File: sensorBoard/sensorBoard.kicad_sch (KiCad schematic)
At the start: 10 parts, among them J1 Conn_01x08, J3 Conn_01x07, J4 Conn_01x04, J5 Conn_01x05, J6 Conn_01x02, J7 Conn_01x04, J8 Conn_01x03, U2 LD1117S33TR_SOT223

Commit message: added the footprints, connectors left
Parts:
- C1, C2: footprint (none) -> Capacitor_SMD:C_0805_2012Metric
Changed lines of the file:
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@@
 			)
 		)
-		(property "Footprint" ""
+		(property "Footprint" "Capacitor_SMD:C_0805_2012Metric"
 			(at 27.94 170.18 0)
 			(effects
@@
 			)
 		)
-		(property "Footprint" ""
+		(property "Footprint" "Capacitor_SMD:C_0805_2012Metric"
 			(at 60.96 168.91 0)
 			(effects

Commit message: started the layout
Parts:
- removed J1: Conn_01x08, symbol Connector_Generic:Conn_01x08
- removed J7: Conn_01x04, symbol Connector_Generic:Conn_01x04
- added H1, H2, H3, H4: MountingHole_Pad, MountingHole:MountingHole_4.3mm_M4_Pad_Via, symbol Mechanical:MountingHole_Pad
- added J1: Conn_01x04, Connector_Phoenix_MC_HighVoltage:PhoenixContact_MCV_1,5_4-G-5.08_1x04_P5.08mm_Vertical, symbol Connector_Generic:Conn_01x04
- added J7: Conn_01x02, Connector_Phoenix_MC_HighVoltage:PhoenixContact_MCV_1,5_2-G-5.08_1x02_P5.08mm_Vertical, symbol Connector_Generic:Conn_01x02
- J3: footprint (none) -> Connector_PinHeader_2.54mm:PinHeader_1x07_P2.54mm_Vertical
- J4: footprint (none) -> Connector_Phoenix_MC_HighVoltage:PhoenixContact_MCV_1,5_4-G-5.08_1x04_P5.08mm_Vertical
- J5: footprint (none) -> heder box:662105145021
- J6: footprint (none) -> heder box:662102145021
- J8: footprint (none) -> heder box:662103145021
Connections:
- net GND: now also H1.1, H2.1, H3.1, H4.1, J1.2 (Pin_2), J1.3 (Pin_3)
- net Protection/12V_IN: now also J1.4 (Pin_4)
- net Protection/5V_IN: now also J1.1 (Pin_1)
- new net Commutation/POLE+: J7.1 (Pin_1)
- new net Commutation/POLE-: J7.2 (Pin_2)
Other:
- sheet Commutation ports: added POLE+, POLE-; removed POLE_1, POLE_1_EN, POLE_2, POLE_2_EN
- sheet microcontroller ports: added none; removed POLE_1_EN, POLE_2_EN

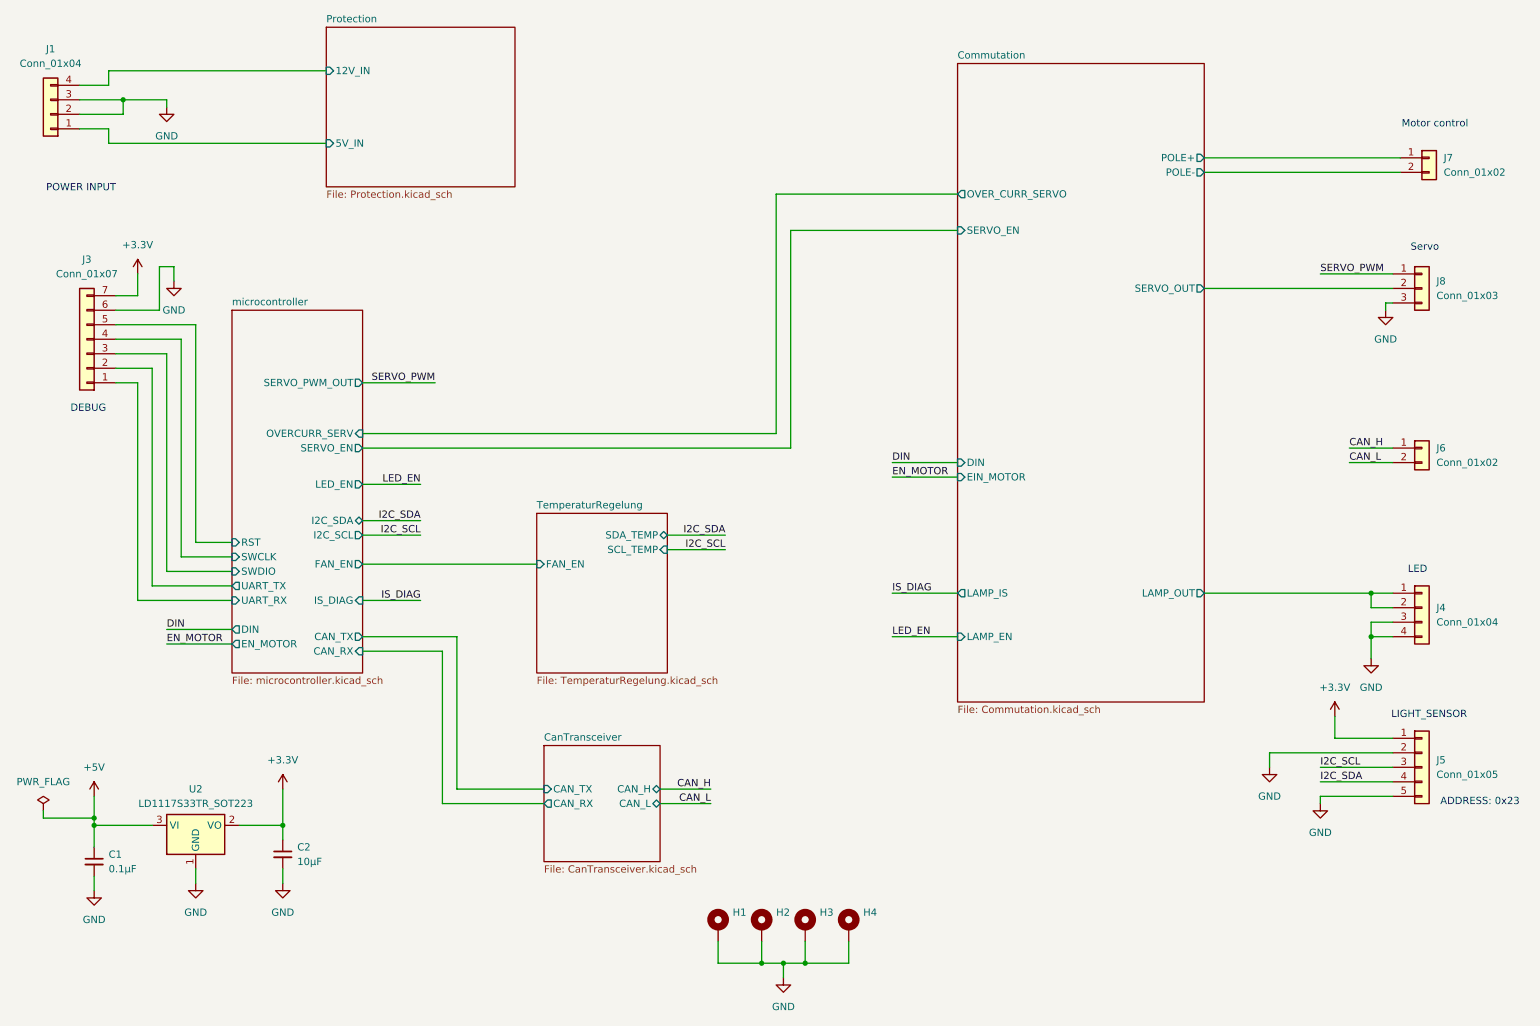
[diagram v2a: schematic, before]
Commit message: new two separate pcbs
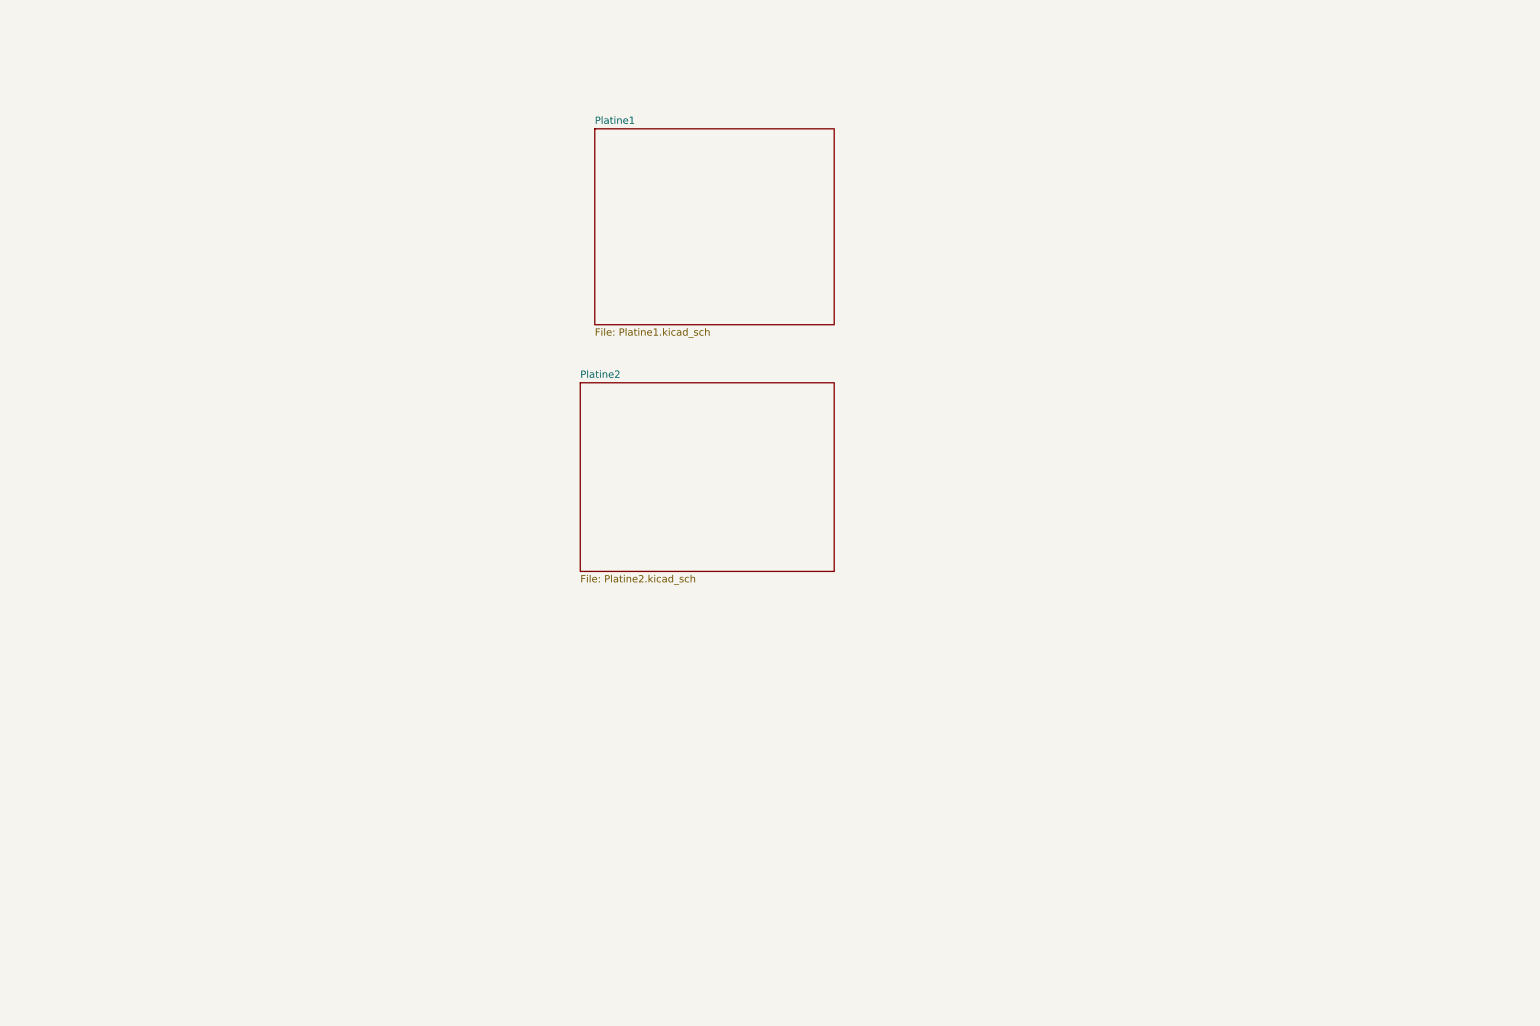
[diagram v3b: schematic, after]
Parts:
- removed C1: 0.1µF, Capacitor_SMD:C_0805_2012Metric, symbol Device:C_Small
- removed C2: 10µF, Capacitor_SMD:C_0805_2012Metric, symbol Device:C_Small
- removed H1, H2, H3, H4: MountingHole_Pad, MountingHole:MountingHole_4.3mm_M4_Pad_Via, symbol Mechanical:MountingHole_Pad
- removed J1, J4: Conn_01x04, Connector_Phoenix_MC_HighVoltage:PhoenixContact_MCV_1,5_4-G-5.08_1x04_P5.08mm_Vertical, symbol Connector_Generic:Conn_01x04
- removed J3: Conn_01x07, Connector_PinHeader_2.54mm:PinHeader_1x07_P2.54mm_Vertical, symbol Connector_Generic:Conn_01x07
- removed J5: Conn_01x05, heder box:662105145021, symbol Connector_Generic:Conn_01x05
- removed J6: Conn_01x02, heder box:662102145021, symbol Connector_Generic:Conn_01x02
- removed J7: Conn_01x02, Connector_Phoenix_MC_HighVoltage:PhoenixContact_MCV_1,5_2-G-5.08_1x02_P5.08mm_Vertical, symbol Connector_Generic:Conn_01x02
- removed J8: Conn_01x03, heder box:662103145021, symbol Connector_Generic:Conn_01x03
- removed U2: LD1117S33TR_SOT223, Package_TO_SOT_SMD:SOT-223-3_TabPin2, symbol Regulator_Linear:LD1117S33TR_SOT223
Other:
- removed sheet CanTransceiver
- removed sheet Commutation
- removed sheet Protection
- removed sheet TemperaturRegelung
- removed sheet microcontroller
- added sheet Platine1 (Platine1.kicad_sch)
- added sheet Platine2 (Platine2.kicad_sch)
- note removed: "ADDRESS: 0x23"
- note removed: "DEBUG"
- note removed: "LED"
- note removed: "LIGHT_SENSOR"
- note removed: "Motor control"
- note removed: "POWER INPUT"
- note removed: "Servo"

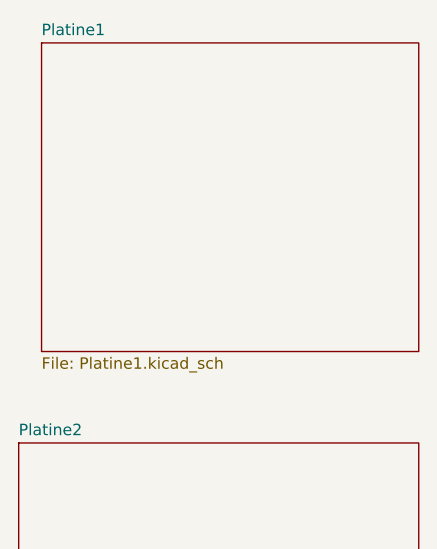
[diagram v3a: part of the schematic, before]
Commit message: Das erstes PCB ist fast fertig. Die Vias waren auf die Platine platziert und Poligon war gefüllt.
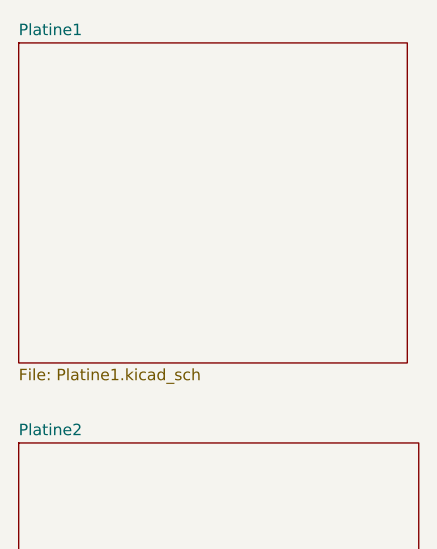
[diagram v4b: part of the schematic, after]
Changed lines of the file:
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@@
 	)
 	(sheet
-		(at 115.57 41.91)
-		(size 41.91 34.29)
+		(at 113.03 41.91)
+		(size 43.18 35.56)
 		(fields_autoplaced yes)
 		(stroke
@@
 		)
 		(property "Sheetname" "Platine1"
-			(at 115.57 41.1984 0)
+			(at 113.03 41.1984 0)
 			(effects
 				(font
@@
 		)
 		(property "Sheetfile" "Platine1.kicad_sch"
-			(at 115.57 76.7846 0)
+			(at 113.03 78.0546 0)
 			(effects
 				(font

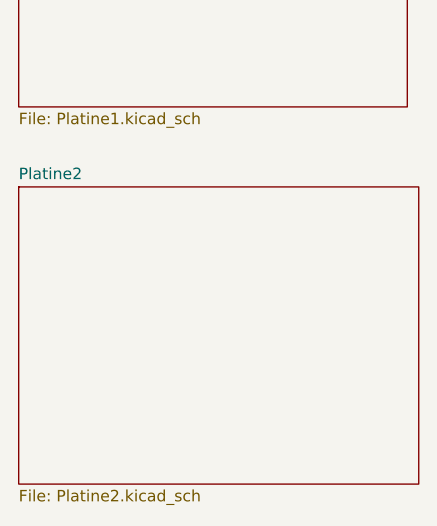
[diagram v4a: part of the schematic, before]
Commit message: added old software + new PCB
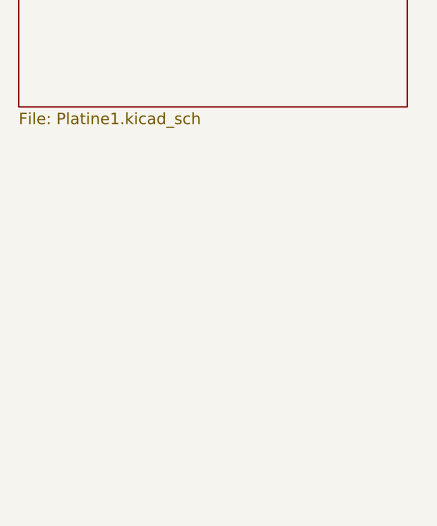
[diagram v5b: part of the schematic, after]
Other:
- removed sheet Platine2
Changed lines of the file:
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@@
 (kicad_sch
-	(version 20231120)
+	(version 20250114)
 	(generator "eeschema")
-	(generator_version "8.0")
+	(generator_version "9.0")
 	(paper "A4")
-	(sheet
-		(at 113.03 86.36)
-		(size 44.45 33.02)
-		(fields_autoplaced yes)
-		(stroke
-			(width 0.1524)
-			(type solid)
-		)
-		(fill
-			(color 0 0 0 0.0000)
-		)
-		(property "Sheetname" "Platine2"
-			(at 113.03 85.6484 0)
-			(effects
-				(font
-					(size 1.27 1.27)
-				)
-				(justify left bottom)
-			)
-		)
-		(property "Sheetfile" "Platine2.kicad_sch"
-			(at 113.03 119.9646 0)
-			(effects
-				(font
-					(size 1.27 1.27)
-				)
-				(justify left top)
-			)
-		)
-		(instances
-			(project "sensorBoard"
-				(path "/df1584e9-54f0-49dc-b423-5f64048efa01"
-					(page "10")
-				)
-			)
-		)
-	)
 	(sheet
 		(at 113.03 41.91)
 		(size 43.18 35.56)
+		(exclude_from_sim no)
+		(in_bom yes)
+		(on_board yes)
+		(dnp no)
 		(fields_autoplaced yes)
 		(stroke
@@
 		)
 	)
+	(embedded_fonts no)
 )
